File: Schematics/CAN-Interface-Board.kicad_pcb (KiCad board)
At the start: 4 copper layers, 50 x 100 mm, 78 parts, among them CN1 Limit Switch Connector 1, CN2 Limit Switch Connector 2, J1 Microsemi_FlashPro-JTAG-10, J2 USB_C_Receptacle, J3 Micro_SD_Card, J4 Screw_Terminal_01x02, J5 Screw_Terminal_01x02, J6 Screw_Terminal_01x03, J7 USB_C_Receptacle, U1 SN65HVD230, U2 LDL1117-3.3, U3 STM32F405RGT6, U4 ESP32-C3-MINI-1-N4, U5 LSM6DS3TR-C, U6 LDL1117-3.3, U7 Bosch BMP388, Y1 8mhz

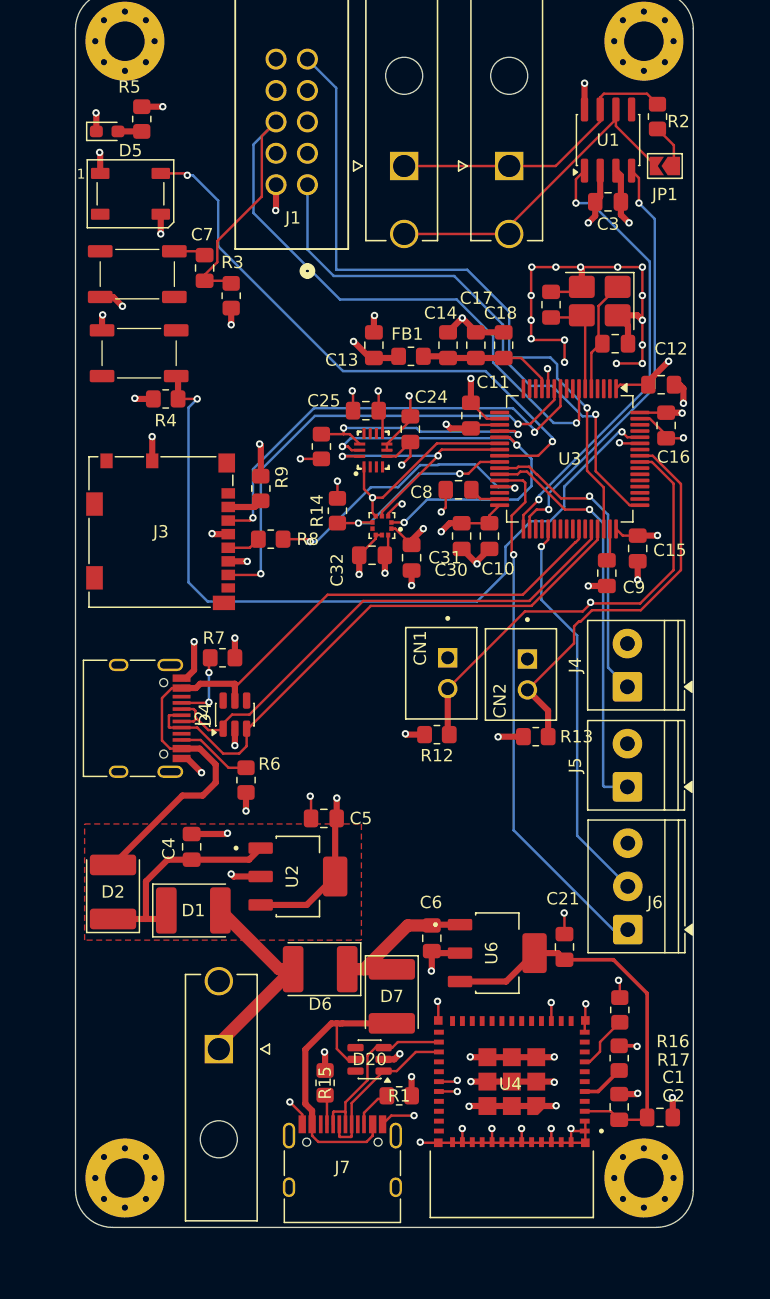
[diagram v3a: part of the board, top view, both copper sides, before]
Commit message: clean up of routing
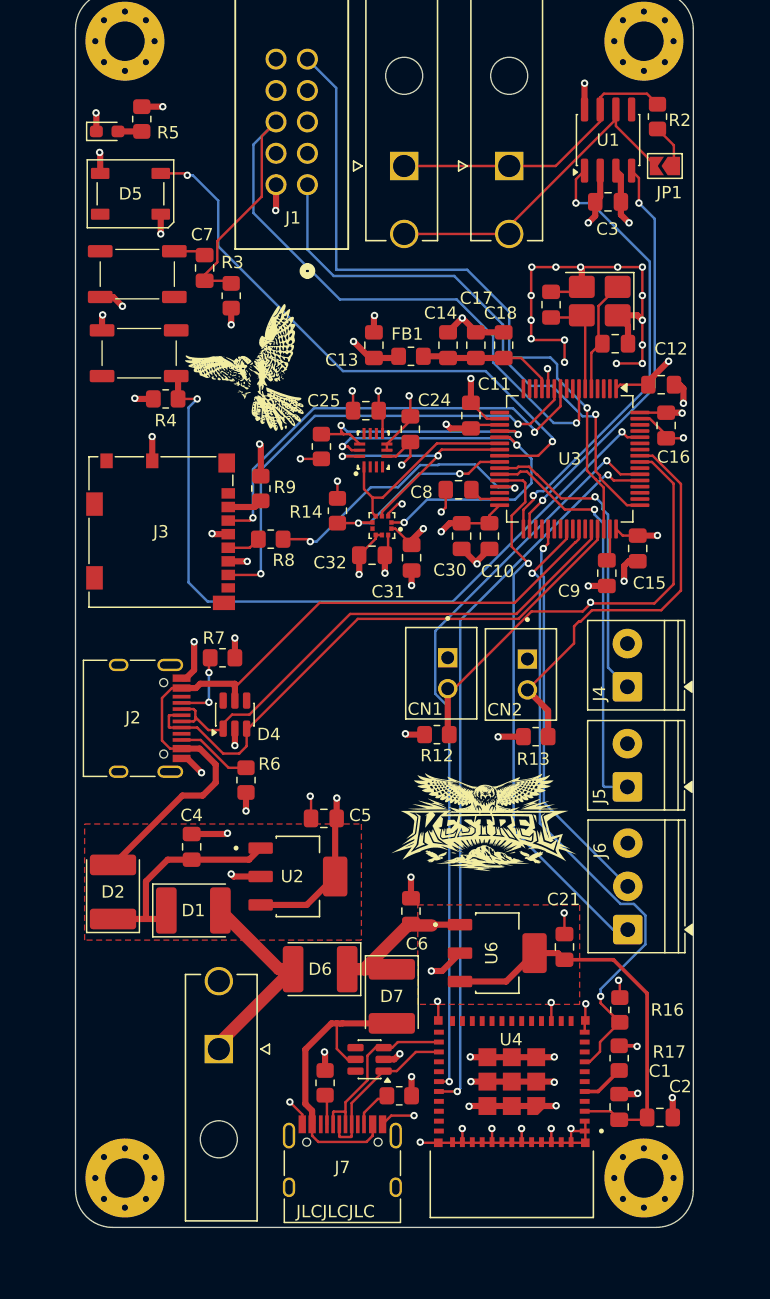
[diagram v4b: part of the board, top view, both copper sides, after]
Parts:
- added G***: LOGO, LOGO, F.Cu at (143.3, 98.4)
- added G***: LOGO, LOGO, F.Cu at (123.8, 60.4)
- moved C6 2.77 mm to (137.2, 104.4), turned to 90 degrees
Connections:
- U3 pad 40: unconnected-(U3-PC9-Pad40) -> /ESP32-C3-Mini/STM-ESP-ON
- U3 pad 53: unconnected-(U3-PC12-Pad53) -> /ESP32-C3-Mini/ESP_RX
- U3 pad 54: unconnected-(U3-PD2-Pad54) -> /ESP32-C3-Mini/ESP_TX
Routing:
- net /ESP32-C3-Mini/ESP_TX: track 1.53 -> 60.5 mm, vias 1 -> 2
- net /ESP32-C3-Mini/ESP_RX: track 1.49 -> 59.3 mm, vias 1 -> 2
- net /ESP32-C3-Mini/STM-ESP-ON: track 4.61 -> 52.4 mm, vias 0 -> 2
- net /MCU/BOOT0: track 63.9 -> 61.7 mm
- net GND: track 186.3 -> 188.0 mm, vias 73 -> 74
- net unconnected-(U3-PB7-Pad59): track 1.67 -> 0.00 mm, vias 1 -> 0
- net /MCU/5Venable: track 43.4 -> 44.5 mm
- net /MCU/LimitSwitchRoll: track 33.0 -> 33.9 mm
- net /MCU/LimitSwitchCAS: track 37.0 -> 37.7 mm
- net /CAN Transciever/CAN_RX_2: track 34.5 -> 34.0 mm
- net /IMU/IMU_CS: track 19.9 -> 20.5 mm
- net /Barometer/Baraometer-MISO: vias 1 -> 0
- added copper zone on F.Cu, net GND
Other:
- board text added: "JLCJLCJLC"

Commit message: updated board waiting on review
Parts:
- added C22: 100nf, Capacitor_SMD:C_0805_2012Metric_Pad1.18x1.45mm_HandSolder, F.Cu at (131.0, 33.3)
- added R11: 10k, Resistor_SMD:R_0805_2012Metric_Pad1.20x1.40mm_HandSolder, F.Cu at (149.4, 93.8)
- C2: value 1uf -> 1u
- J1: footprint myFootprints:CONN_7024610XX_MOL -> Connector_PinHeader_1.27mm:PinHeader_2x05_P1.27mm_Vertical
- J4, J5: footprint TerminalBlock_Phoenix:TerminalBlock_Phoenix_PT-1,5-2-3.5-H_1x02_P3.50mm_Horizontal -> Connector_JST:JST_XH_B2B-XH-AM_1x02_P2.50mm_Vertical
- J6: footprint TerminalBlock_Phoenix:TerminalBlock_Phoenix_PT-1,5-3-3.5-H_1x03_P3.50mm_Horizontal -> Connector_JST:JST_EH_B3B-EH-A_1x03_P2.50mm_Vertical
- moved J1 13.8 mm to (126.9, 32.0), turned to 0 degrees
- moved J6 2.40 mm to (157.1, 105.8)
- moved G*** 2.16 mm to (141.2, 98.5)
- moved R13 1.67 mm to (146.4, 91.8)
- moved J5 1.33 mm to (155.9, 94.7)
- moved J4 1.26 mm to (155.9, 86.2)
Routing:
- net /MCU/SWCLK: track 45.3 -> 60.6 mm, vias 1 -> 2
- net /MCU/NRST: track 62.9 -> 57.4 mm, vias 1 -> 2
- net /MCU/CurrentCheck: track 32.1 -> 36.5 mm, vias 1 -> 2
- net +3.3V: track 77.1 -> 80.9 mm, vias 22 -> 23
- net /ESP32-C3-Mini/STM-ESP-ON: track 52.4 -> 50.1 mm
- net /MCU/SWDIO: track 56.1 -> 58.4 mm, vias 1 -> 2
- net /MCU/LimitSwitchRoll: track 33.9 -> 36.2 mm
- net /MCU/5Venable: track 44.5 -> 46.6 mm, vias 1 -> 2
- net GND: track 188.0 -> 189.6 mm, vias 74 -> 75
- net /MCU/PWMServo_CAS: track 33.7 -> 35.1 mm
- net /MCU/PWMServo_Roll: track 25.3 -> 26.6 mm
- net /MCU/LimitSwitchCAS: track 37.7 -> 37.3 mm, vias 1 -> 0
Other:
- board text added: "+3V"
- board text added: "AIR"
- board text added: "BATT"
- board text added: "Buck On"
- board text added: "GND"
- board text added: "LS AIR"
- board text added: "LS ROLL"
- board text added: "Made by Reed"
- board text added: "Pwr"
- board text added: "ROLL"

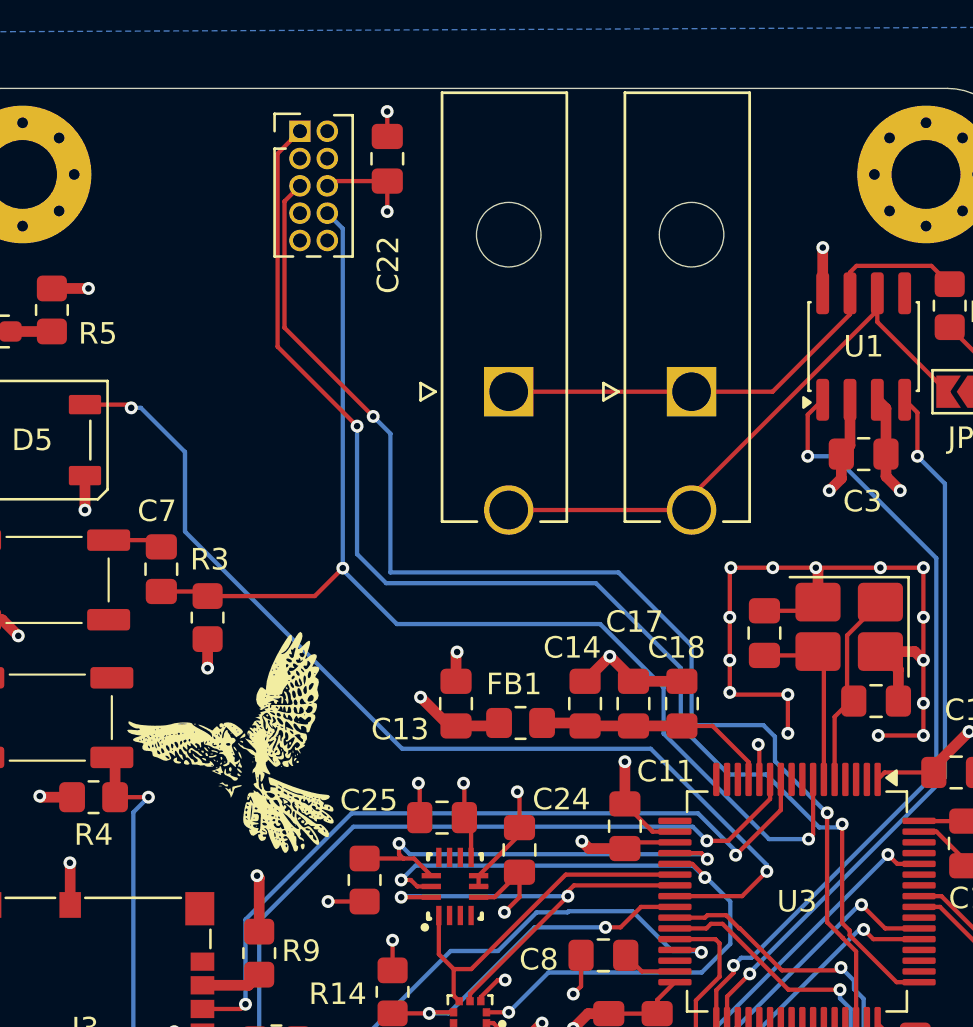
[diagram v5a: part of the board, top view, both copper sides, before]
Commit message: Updating to KiCad 10.0
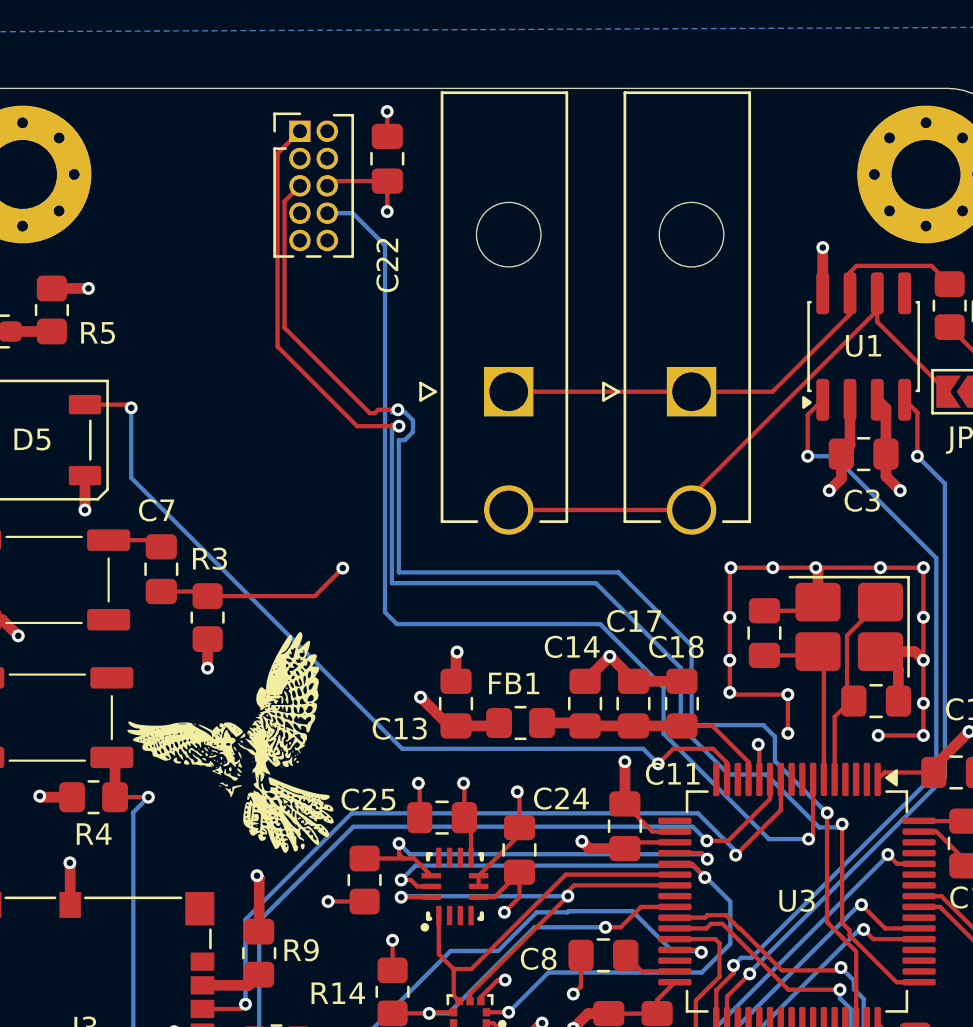
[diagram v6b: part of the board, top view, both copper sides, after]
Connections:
- U3 pad 15: unconnected-(U3-PA1-Pad15) -> /MCU/RGB_DATA
- U3 pad 24: /MCU/RGB_DATA -> unconnected-(U3-PC4-Pad24)
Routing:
- net /MCU/RGB_DATA: track 47.8 -> 40.0 mm
- net /MCU/SWDIO: track 58.4 -> 60.7 mm
- net /MCU/SWCLK: track 60.6 -> 62.4 mm
- net /MCU/NRST: track 57.4 -> 58.1 mm

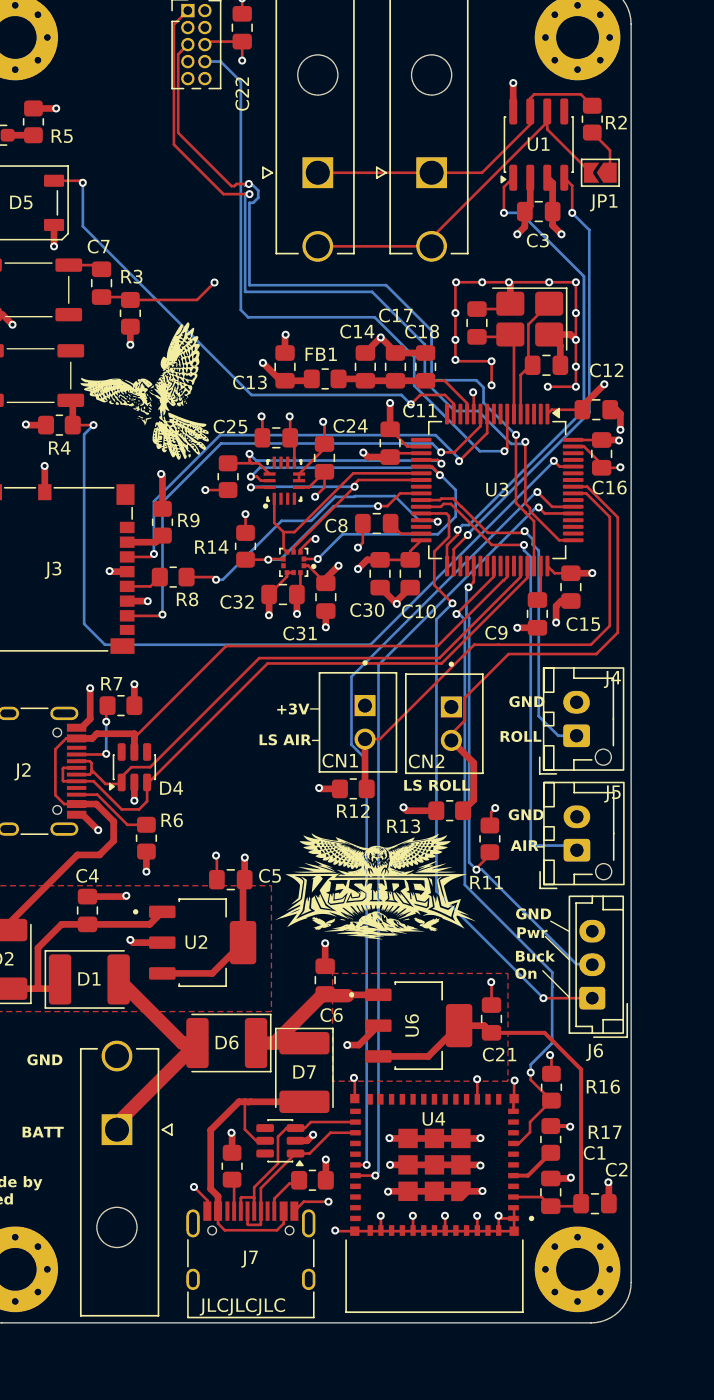
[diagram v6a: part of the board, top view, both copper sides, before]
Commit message: removed esp32 to seperate board, added gps breakout, pending final review for purchase
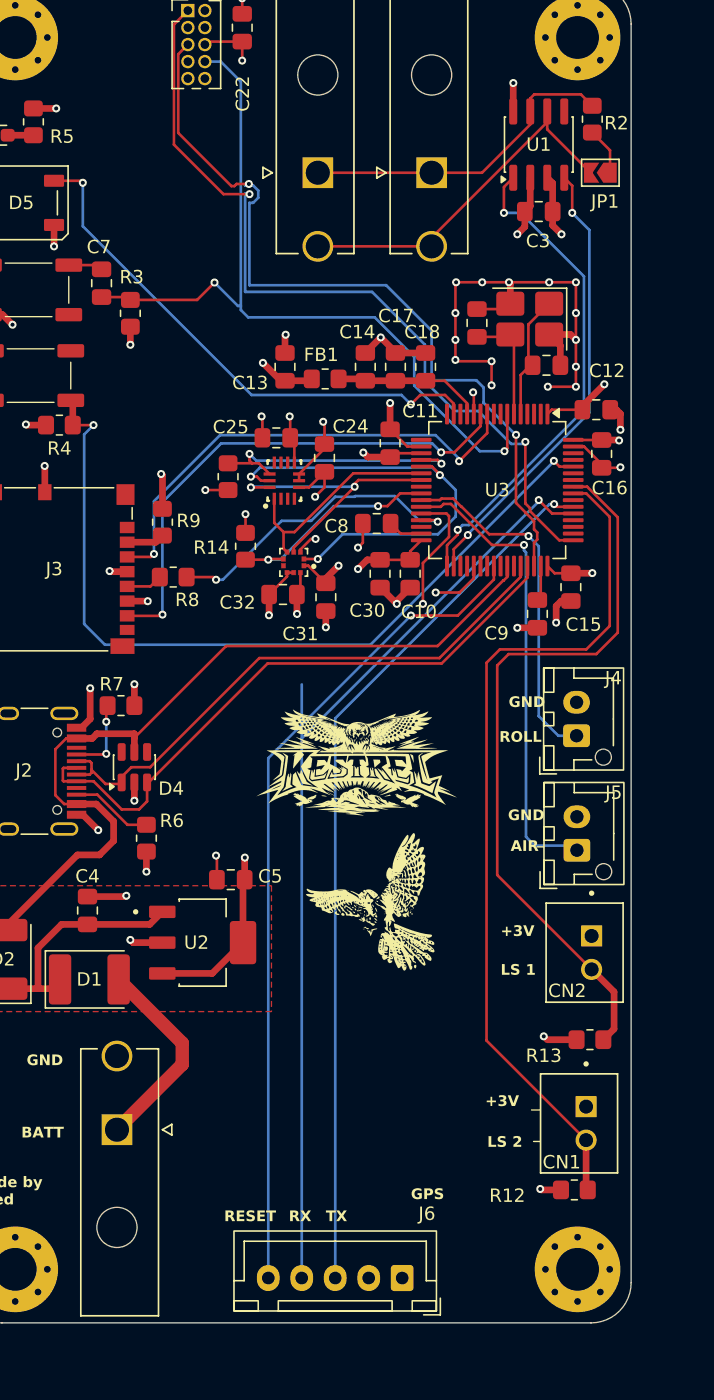
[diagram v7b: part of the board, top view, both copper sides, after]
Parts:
- removed C1: 100nf, Capacitor_SMD:C_0805_2012Metric_Pad1.18x1.45mm_HandSolder
- removed C2, C6: 1u, Capacitor_SMD:C_0805_2012Metric_Pad1.18x1.45mm_HandSolder
- removed C21: 4.7u, Capacitor_SMD:C_0805_2012Metric_Pad1.18x1.45mm_HandSolder
- removed D20: SRV05-4.TCT, Package_TO_SOT_SMD:SOT-23-6
- removed D6, D7: D_Schottky, Diode_SMD:D_2114_3652Metric
- removed J7: USB_C_Receptacle, Connector_USB:USB_C_Receptacle_HRO_TYPE-C-31-M-12
- removed R1, R15: 5.1k, Resistor_SMD:R_0805_2012Metric_Pad1.20x1.40mm_HandSolder
- removed R11, R16, R17: 10k, Resistor_SMD:R_0805_2012Metric_Pad1.20x1.40mm_HandSolder
- removed U4: ESP32-C3-MINI-1-N4, myFootprints:XCVR_ESP32-C3-MINI-1-N4
- removed U6: LDL1117-3.3, myFootprints:SOT230P700X180-4N
- J6: value Screw_Terminal_01x03 -> Conn_01x05_Pin; footprint Connector_JST:JST_EH_B3B-EH-A_1x03_P2.50mm_Vertical -> Connector_JST:JST_XH_B5B-XH-A_1x05_P2.50mm_Vertical
- R4: value 100k -> 10k
- moved G*** 41.7 mm to (140.7, 98.5)
- moved CN1 34.2 mm to (156.1, 115.1)
- moved R12 34.2 mm to (155.8, 120.1)
- moved J6 25.3 mm to (142.9, 126.7), turned to 180 degrees
- moved R13 20.1 mm to (156.9, 108.8)
- moved CN2 20.1 mm to (156.5, 102.3)
- moved G*** 9.36 mm to (139.8, 89.3)
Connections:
- J6 pad 1: /MCU/5Venable -> +3.3V
- J6 pad 2: /MCU/CurrentCheck -> GND
- J6 pad 3: GND -> /GPS1_TX
- U3 pad 40: /ESP32-C3-Mini/STM-ESP-ON -> /RESET1
- U3 pad 53: /ESP32-C3-Mini/ESP_RX -> /GPS1_RX
- U3 pad 54: /ESP32-C3-Mini/ESP_TX -> /GPS1_TX
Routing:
- net /GPS1_RX: track 0.00 -> 72.5 mm, vias 0 -> 1
- net GND: track 189.6 -> 120.2 mm, vias 75 -> 49
- net /GPS1_TX: track 0.00 -> 66.3 mm, vias 0 -> 1
- net /RESET1: track 0.00 -> 62.2 mm, vias 0 -> 1
- net /ESP32-C3-Mini/ESP_TX: track 60.5 -> 0.00 mm, vias 2 -> 0
- net /ESP32-C3-Mini/ESP_RX: track 59.3 -> 0.00 mm, vias 2 -> 0
- net /ESP32-C3-Mini/STM-ESP-ON: track 50.1 -> 0.00 mm, vias 2 -> 0
- net /MCU/5Venable: track 46.6 -> 9.52 mm, vias 2 -> 1
- net /ESP32-C3-Mini/ESPPower: track 32.9 -> 0.00 mm
- net /MCU/CurrentCheck: track 36.5 -> 4.20 mm, vias 2 -> 1
- net /MCU/LimitSwitchCAS: track 37.3 -> 64.6 mm
- net /ESP32-C3-Mini/ESP5vUSB: track 25.5 -> 0.00 mm
- net /MCU/LimitSwitchRoll: track 36.2 -> 54.8 mm
- net /ESP32-C3-Mini/D-: track 14.6 -> 0.00 mm
- net Net-(D6-K): track 13.5 -> 0.00 mm
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- removed copper zone on F.Cu, net GND
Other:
- board text added: "GPS"
- board text added: "LS 1"
- board text added: "LS 2"
- board text added: "RESET"
- board text added: "RX"
- board text added: "TX"
- board text removed: "Buck On"
- board text removed: "JLCJLCJLC"
- board text removed: "LS AIR"
- board text removed: "LS ROLL"
- board text removed: "Pwr"

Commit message: finished waiting for review
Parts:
- added C1: 100nf, Capacitor_SMD:C_0805_2012Metric_Pad1.18x1.45mm_HandSolder, F.Cu at (126.7, 80.8)
- added D3: D_Schottky, Diode_SMD:D_SOD-123, F.Cu at (150.2, 88.0)
- added D6: D_Schottky, Diode_SMD:D_SOD-123, F.Cu at (150.4, 96.5)
- added R1: 27r, Resistor_SMD:R_0805_2012Metric_Pad1.20x1.40mm_HandSolder, F.Cu at (136.2, 84.3)
- added R11: 27r, Resistor_SMD:R_0805_2012Metric_Pad1.20x1.40mm_HandSolder, F.Cu at (136.4, 80.8)
- moved G*** 15.8 mm to (136.3, 113.8)
- moved G*** 4.33 mm to (136.4, 92.0)
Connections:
- D4 pad 1: /MCU/D- -> /USB Type C/D-
- D4 pad 3: /MCU/D+ -> /USB Type C/D+
- J2 pad A6: /MCU/D+ -> /USB Type C/D+
- J2 pad A7: /MCU/D- -> /USB Type C/D-
- J2 pad B6: /MCU/D+ -> /USB Type C/D+
- J2 pad B7: /MCU/D- -> /USB Type C/D-
- J4 pad 1: /MCU/PWMServo_Roll -> Net-(D3-K)
- J5 pad 1: /MCU/PWMServo_CAS -> Net-(D6-K)
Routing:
- net /MCU/D+: track 46.3 -> 20.1 mm
- net /MCU/D-: track 43.1 -> 17.9 mm
- net /USB Type C/D+: track 0.00 -> 24.4 mm
- net /USB Type C/D-: track 0.00 -> 23.4 mm
- net /MCU/LimitSwitchRoll: track 54.8 -> 62.0 mm
- net /MCU/LimitSwitchCAS: track 64.6 -> 69.8 mm
- net Net-(D6-K): track 0.00 -> 5.09 mm
- net Net-(D3-K): track 0.00 -> 4.81 mm
- net /GPS1_RX: track 72.5 -> 68.4 mm
- net /MCU/SWDIO: track 60.9 -> 56.9 mm
- net /MCU/PWMServo_Roll: track 26.4 -> 28.8 mm, vias 1 -> 2
- net GND: track 120.2 -> 122.4 mm, vias 49 -> 50
- net /MCU/SWCLK: track 62.4 -> 60.2 mm
- net /USB5V: track 62.4 -> 64.3 mm
- net /MCU/NRST: track 60.8 -> 59.4 mm
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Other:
- board text added: "PWM 1"
- board text added: "PWM 2"
- board text removed: "AIR"
- board text removed: "ROLL"
